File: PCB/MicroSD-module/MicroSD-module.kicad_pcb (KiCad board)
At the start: 2 copper layers, 24.4 x 41.9 mm, 14 parts, among them J1 Connector, K1 HYC77-TF09-200, U1 SE5218, U2 TXB0104PWR

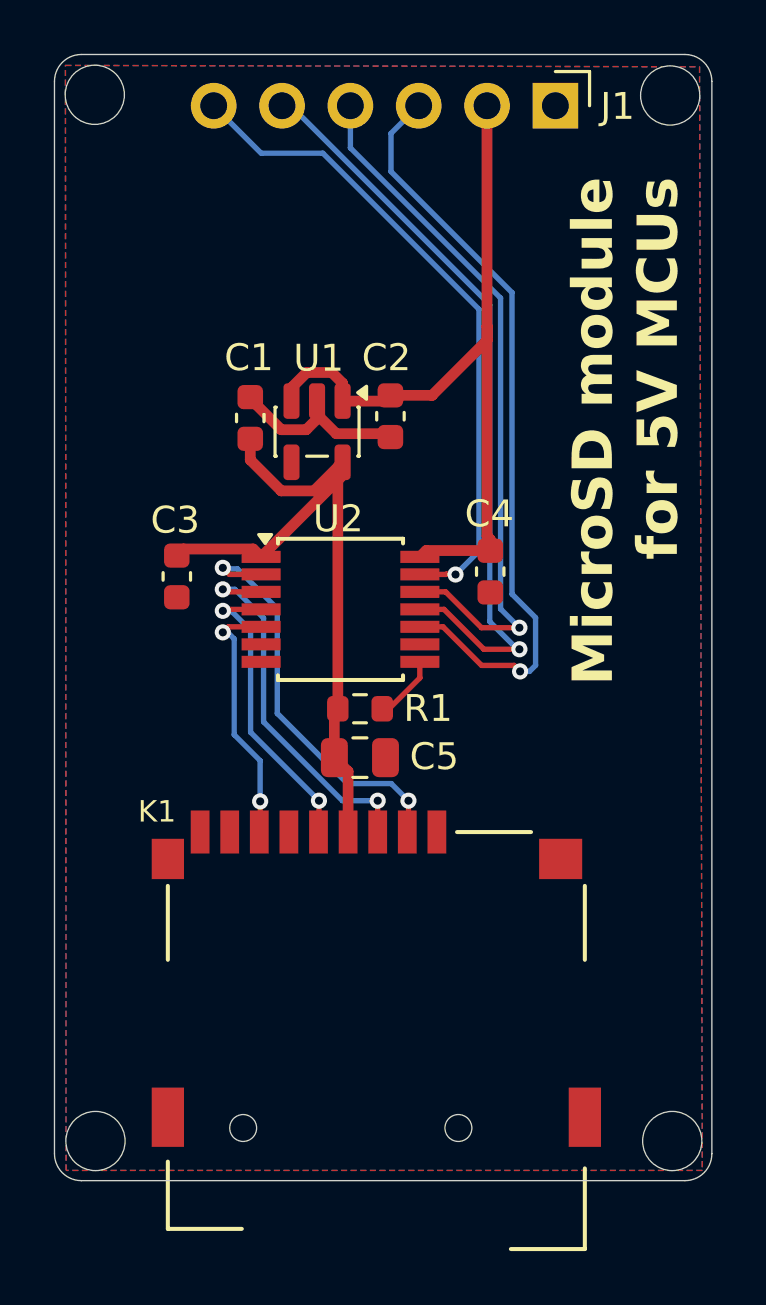
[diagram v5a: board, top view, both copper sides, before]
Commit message: Fix holes placement, off by just a little bit
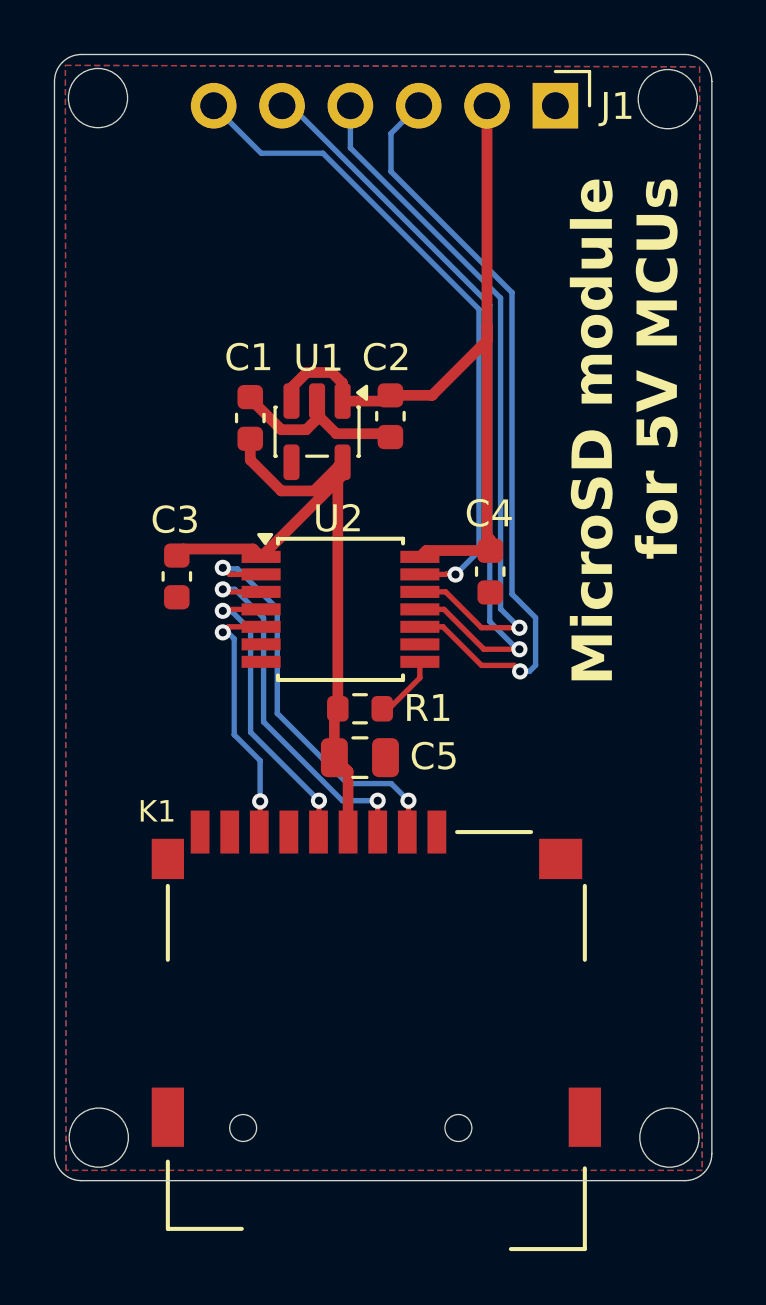
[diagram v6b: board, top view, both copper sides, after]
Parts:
- moved REF**3 0.18 mm to (121.8, 138.7)
- moved REF**1 0.17 mm to (121.8, 100.0)
- moved REF**4 0.16 mm to (143.1, 138.7)
- moved REF**2 0.16 mm to (143.0, 100.1)

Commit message: Update details
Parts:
- moved R1 9.50 mm to (135.9, 114.3), turned to 90 degrees
- moved C4 8.94 mm to (128.7, 113.1), turned to -90 degrees
- moved C2 7.95 mm to (124.7, 111.9), turned to 0 degrees
- moved C1 6.37 mm to (124.7, 117.7), turned to 0 degrees
- moved U1 5.74 mm to (124.7, 114.8)
- moved U2 4.84 mm to (132.3, 114.4), turned to 90 degrees
- moved C3 4.32 mm to (128.7, 116.0)
- moved C5 1.45 mm to (130.2, 125.0), turned to 0 degrees
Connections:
- U2 pad 10: MISO -> CS
- U2 pad 11: SCK -> MOSI
- U2 pad 12: MOSI -> SCK
- U2 pad 13: CS -> MISO
- U2 pad 2: CS_L -> MISO_L
- U2 pad 3: MOSI_L -> SCLK_L
- U2 pad 4: SCLK_L -> MOSI_L
- U2 pad 5: MISO_L -> CS_L
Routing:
- net GND: track 7.24 -> 28.4 mm
- net MISO: track 28.5 -> 12.3 mm
- net SCK: track 28.4 -> 12.4 mm
- net MOSI: track 26.3 -> 13.4 mm
- net CS: track 24.5 -> 15.1 mm
- net CS_L: track 15.5 -> 10.3 mm, vias 2 -> 0
- net 3V3: track 27.3 -> 30.9 mm, vias 0 -> 2
- net MOSI_L: track 14.0 -> 10.8 mm, vias 2 -> 0
- net 5V_burgerDisk: track 29.6 -> 27.8 mm
- net MISO_L: track 9.73 -> 11.3 mm, vias 2 -> 0
- net SCLK_L: track 11.5 -> 10.6 mm, vias 2 -> 0
